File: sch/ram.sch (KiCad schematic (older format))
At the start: 49 parts

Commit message: More precise version. PCB needs a lot of work.
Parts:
- D1, D10, D11, D12, D13, D14, D15, D16, D2, D20, D21, D22, D23, D24, D3, D4, D5, D6, D7, D8, D9: footprint MyLib:DIP-16 -> MyLib_metric:DIP-16
- D36, D40, D41, D42, D43, D44, D75, D85: footprint MyLib:DIP-14 -> MyLib_metric:DIP-14
- D45, D46, D47, D48: footprint MyLib:DIP-20 -> MyLib_metric:DIP-20
- R24, R39, R40, R41, R42, R43, R44, R45, R46, R7, R77, R78, R79, R8, R80, R9: footprint MyLib:Resistor_Horizontal_RM7.5mm -> MyLib_metric:Resistor_Horizontal_RM7.5mm

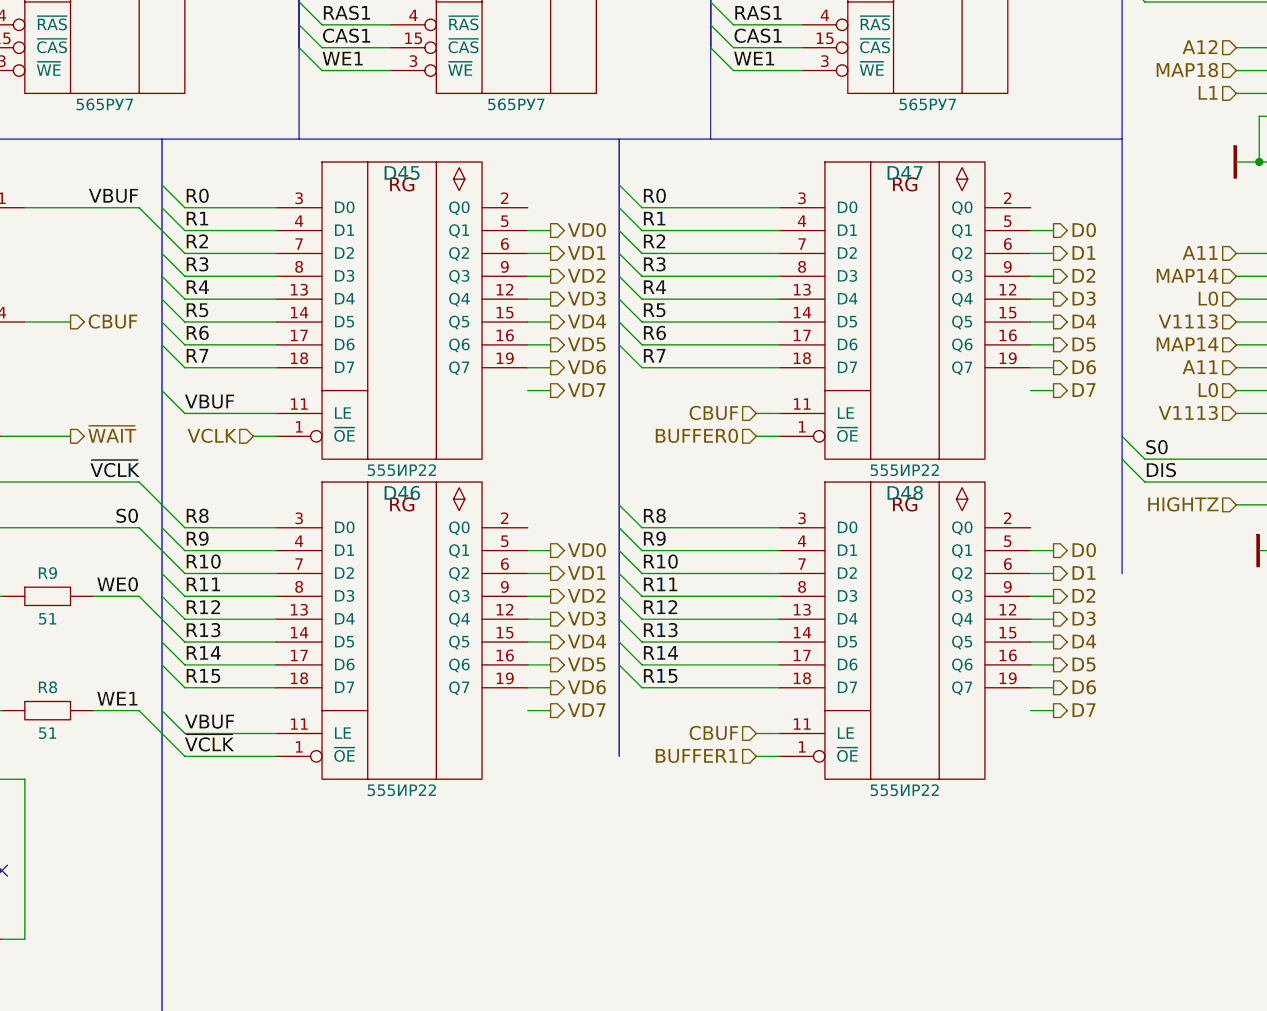
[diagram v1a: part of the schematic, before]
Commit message: IR22 and IR23 symbols updated, part values updated
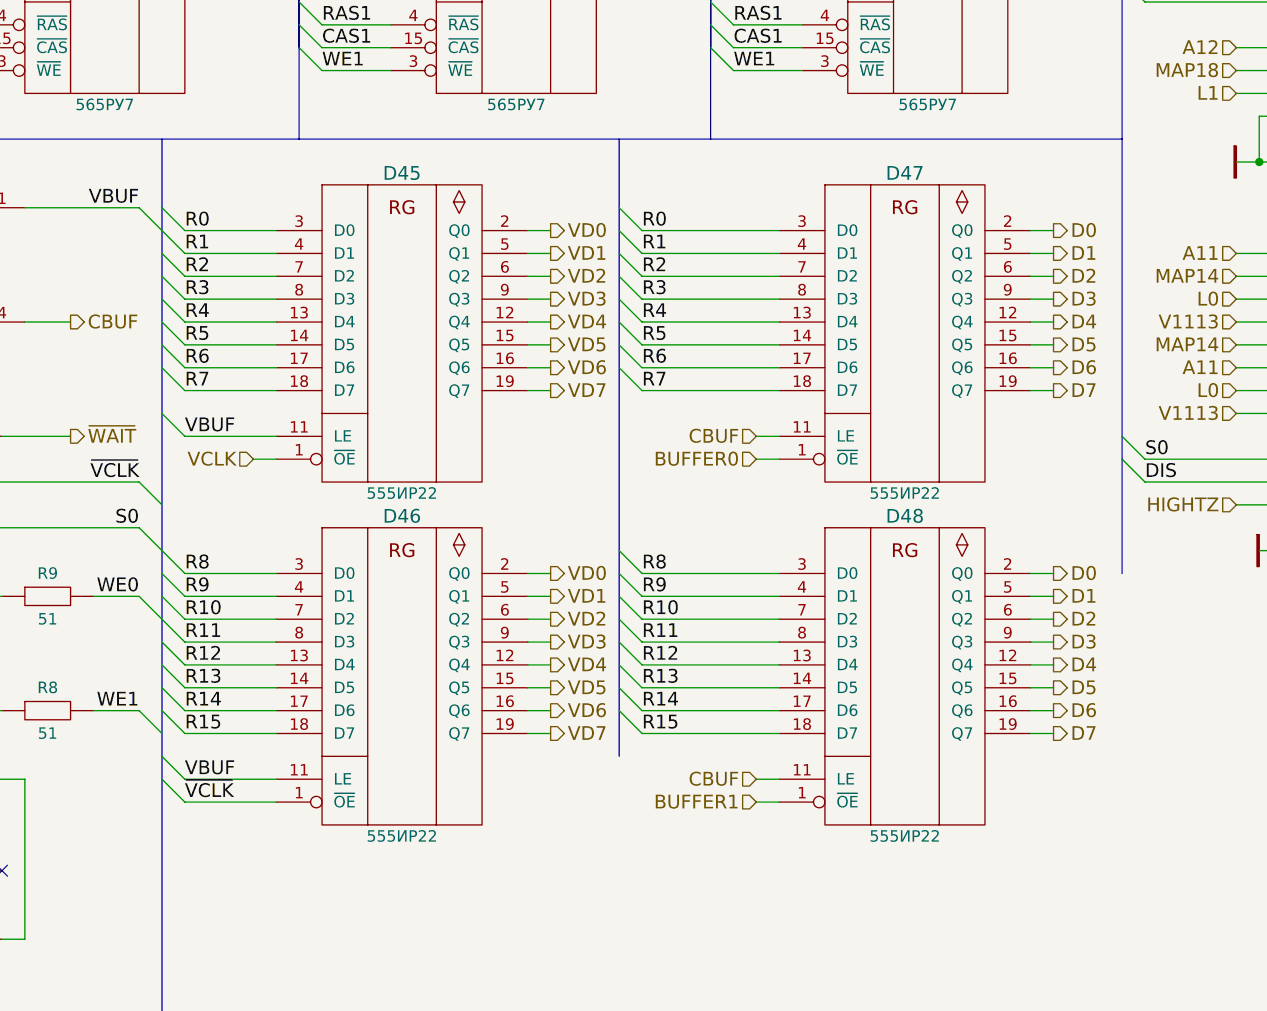
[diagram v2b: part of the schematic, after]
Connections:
- net D0: now also D47.2 (Q0), D48.2 (Q0); no longer D47.5 (Q1), D48.5 (Q1)
- net D1: now also D47.5 (Q1), D48.5 (Q1); no longer D47.6 (Q2), D48.6 (Q2)
- net D2: now also D47.6 (Q2), D48.6 (Q2); no longer D47.9 (Q3), D48.9 (Q3)
- net D3: now also D47.9 (Q3), D48.9 (Q3); no longer D47.12 (Q4), D48.12 (Q4)
- net D4: now also D47.12 (Q4), D48.12 (Q4); no longer D47.15 (Q5), D48.15 (Q5)
- net D5: now also D47.15 (Q5), D48.15 (Q5); no longer D47.16 (Q6), D48.16 (Q6)
- net D6: now also D47.16 (Q6), D48.16 (Q6); no longer D47.19 (Q7), D48.19 (Q7)
- net D7: now also D47.19 (Q7), D48.19 (Q7)
- net VD0: now also D45.2 (Q0), D46.2 (Q0); no longer D45.5 (Q1), D46.5 (Q1)
- net VD1: now also D45.5 (Q1), D46.5 (Q1); no longer D45.6 (Q2), D46.6 (Q2)
- net VD2: now also D45.6 (Q2), D46.6 (Q2); no longer D45.9 (Q3), D46.9 (Q3)
- net VD3: now also D45.9 (Q3), D46.9 (Q3); no longer D45.12 (Q4), D46.12 (Q4)
- net VD4: now also D45.12 (Q4), D46.12 (Q4); no longer D45.15 (Q5), D46.15 (Q5)
- net VD5: now also D45.15 (Q5), D46.15 (Q5); no longer D45.16 (Q6), D46.16 (Q6)
- net VD6: now also D45.16 (Q6), D46.16 (Q6); no longer D45.19 (Q7), D46.19 (Q7)
- net VD7: now also D45.19 (Q7), D46.19 (Q7)
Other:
- moved on the sheet: D45, D46, D47, D48
